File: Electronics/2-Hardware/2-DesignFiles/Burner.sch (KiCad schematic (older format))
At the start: 52 parts, among them P1 CONN_2, P2 CONN_2, P3 CONN_1, P4 CONN_01X03, P5 CONN_01X04, P6 CONN_1, P7 CONN_4, Q1 IRF9310, Q2 IRLML6402, Q3 IRL6342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

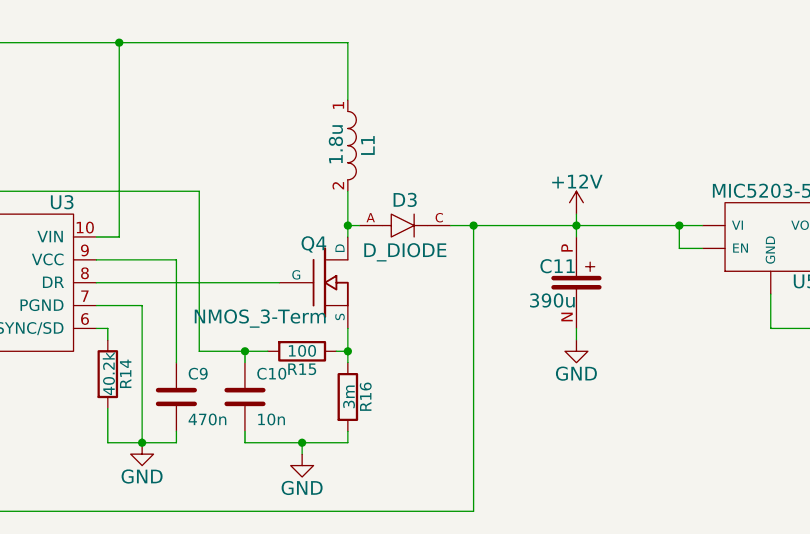
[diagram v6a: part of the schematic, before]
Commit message: Added diode and inductor for Boost converter
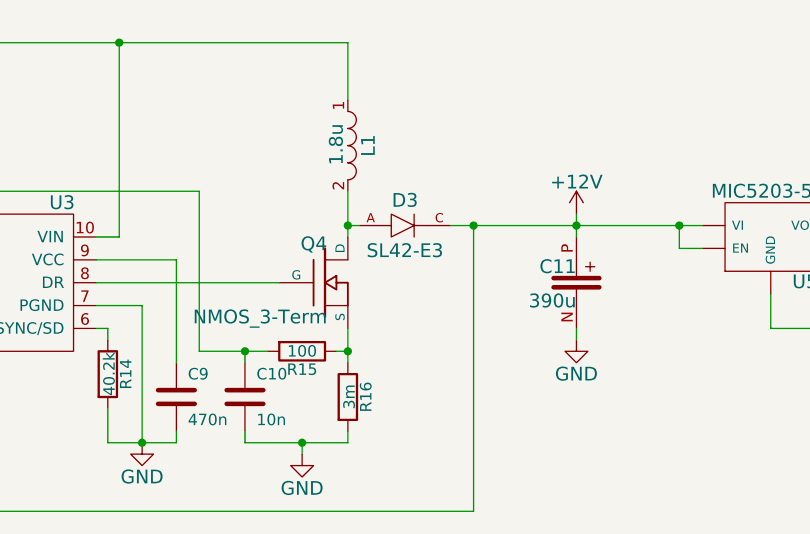
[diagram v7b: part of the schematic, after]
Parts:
- D3: value D_DIODE -> SL42-E3; footprint (none) -> Diodes:DIODE_DO214AB-SMC; DigikeyNumber (none) -> SL42-E3/57TGICT-ND; Manufacturer (none) -> Vishay; ManufacturerNumber (none) -> SL42-E3/57T
- L1: footprint (none) -> Inductors:IND_BOURNS_SRP1238A; DigikeyNumber (none) -> SRP1238A-1R8MCT-ND; Manufacturer (none) -> Bourns; ManufacturerNumber (none) -> SRP1238A-1R8M
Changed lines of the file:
@@
 P 7300 1600
 F 0 "D3" V 7190 1600 60  0000 C CNN
-F 1 "D_DIODE" V 7410 1600 60  0000 C CNN
-F 2 "" H 7300 1580 60  0001 C CNN
-F 3 "" H 7300 1580 60  0001 C CNN
+F 1 "SL42-E3" V 7410 1600 60  0000 C CNN
+F 2 "Diodes:DIODE_DO214AB-SMC" H 7300 1580 60  0001 C CNN
+F 3 "http://www.vishay.com/docs/88742/sl42.pdf" H 7300 1580 60  0001 C CNN
+F 4 "SL42-E3/57TGICT-ND" V 7300 1600 60  0001 C CNN "DigikeyNumber"
+F 5 "Vishay" V 7300 1600 60  0001 C CNN "Manufacturer"
+F 6 "SL42-E3/57T" V 7300 1600 60  0001 C CNN "ManufacturerNumber"
 	1    7300 1600
 	0    1    1    0
@@
 F 0 "L1" V 7140 1250 60  0000 C CNN
 F 1 "1.8u" V 7000 1255 60  0000 C CNN
-F 2 "" H 7050 1250 60  0001 C CNN
-F 3 "" H 7050 1250 60  0000 C CNN
+F 2 "Inductors:IND_BOURNS_SRP1238A" H 7050 1250 60  0001 C CNN
+F 3 "http://www.bourns.com/data/global/pdfs/SRP1238A.pdf" H 7050 1250 60  0001 C CNN
+F 4 "SRP1238A-1R8MCT-ND" V 7050 1250 60  0001 C CNN "DigikeyNumber"
+F 5 "Bourns" V 7050 1250 60  0001 C CNN "Manufacturer"
+F 6 "SRP1238A-1R8M" V 7050 1250 60  0001 C CNN "ManufacturerNumber"
 	1    7050 1250
 	1    0    0    -1

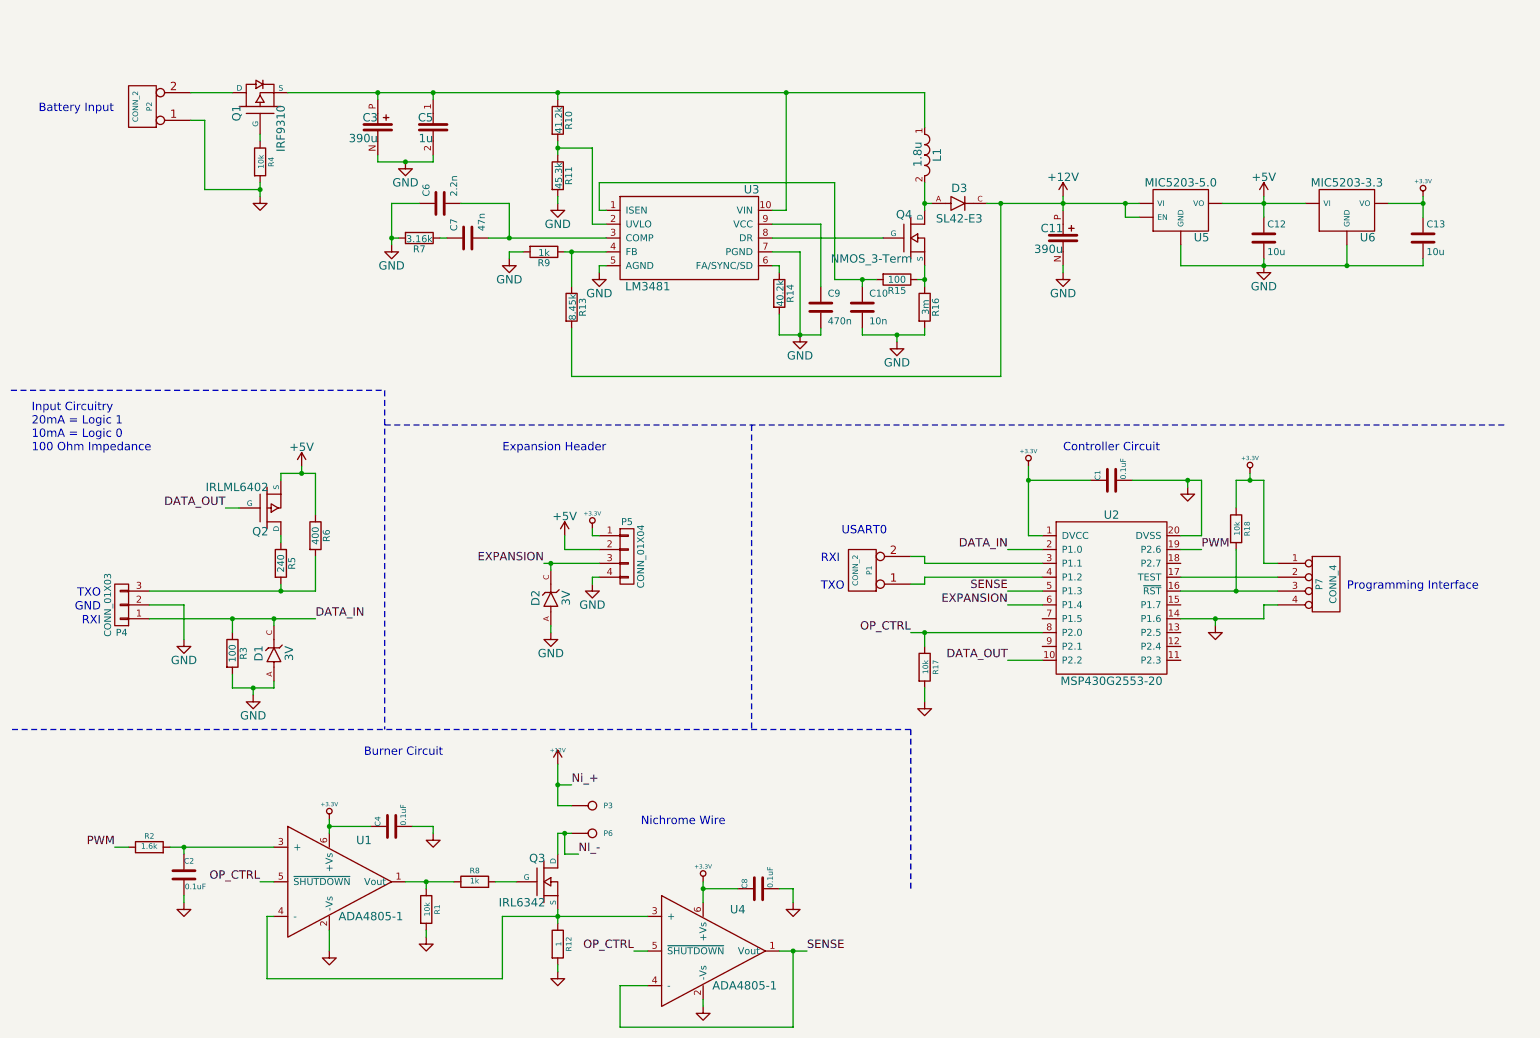
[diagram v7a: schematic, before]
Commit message: Updated schematic with LEDs, created board layout
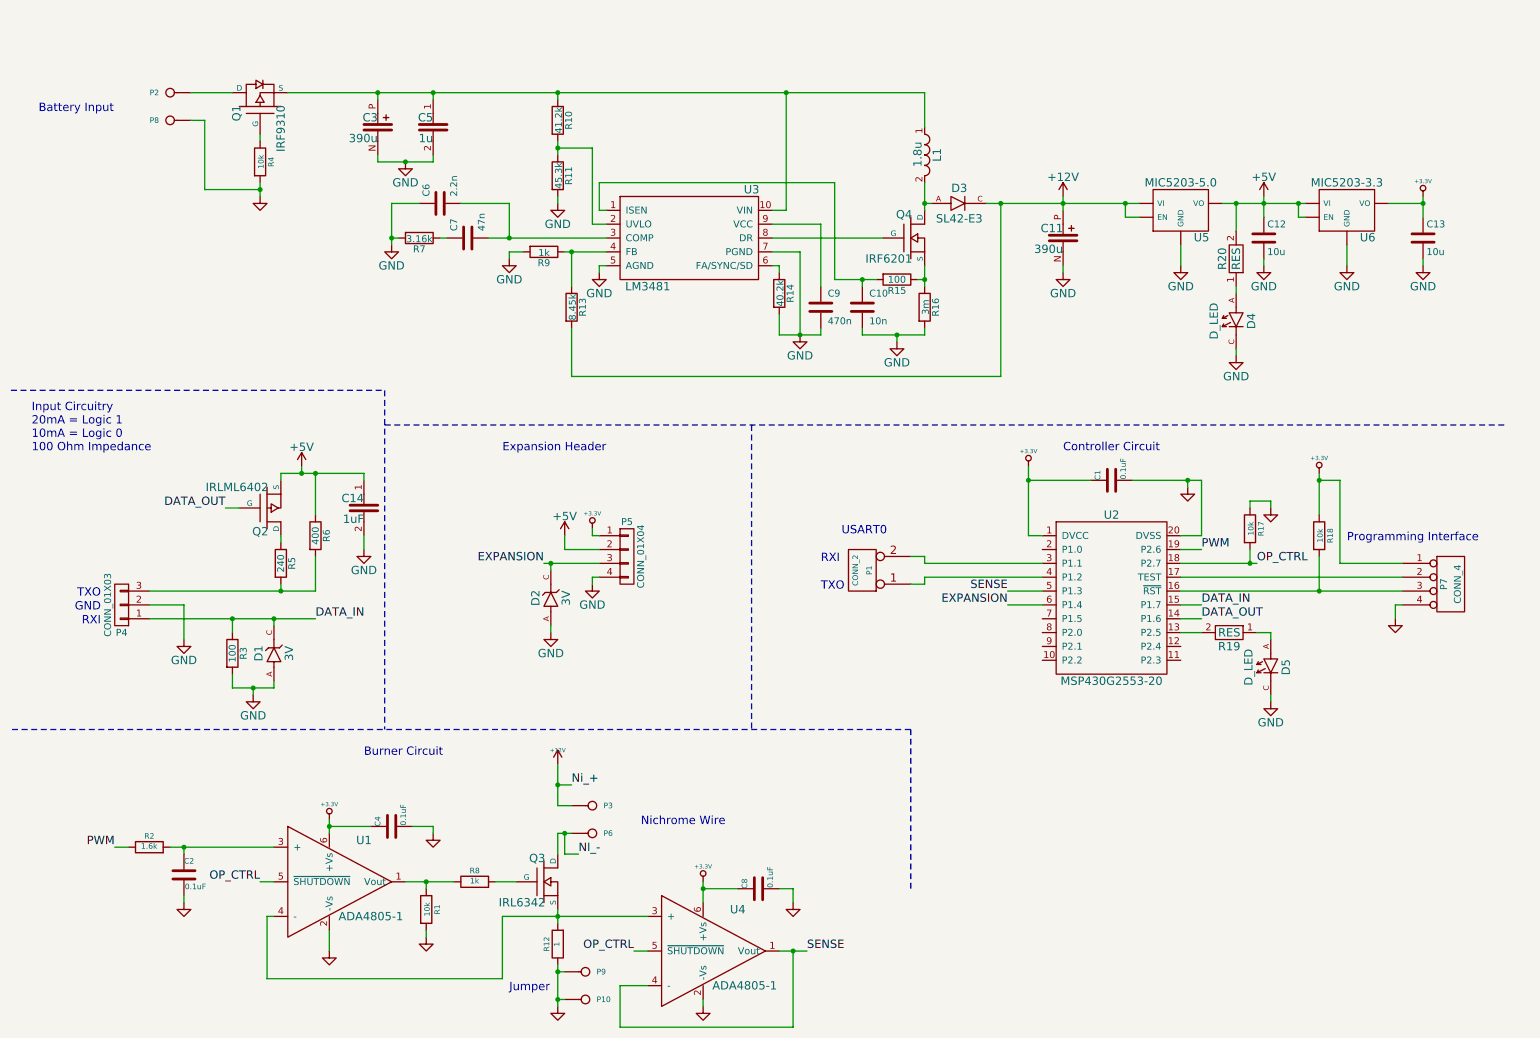
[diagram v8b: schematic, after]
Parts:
- removed P2: CONN_2, Footprints:CONN_1x2, symbol CONN_2
- removed U6: MIC5203-3.3, SMD:SOT-23-5, symbol LINEAR_REGULATOR
- added C14: 1uF, SMD:SMD_0805, symbol CAP
- added D4, D5: D_LED, LEDs:LED_1206, symbol D_LED
- added P10, P2, P8, P9: CONN_1, Connectors:CONN_2.54mm_1x1, symbol CONN_1
- added R19, R20: RES, SMD:SMD_0805, symbol RES
- added U6: MIC5203-3.3, SMD:SOT-23-5, symbol LINEAR_REGULATOR_EN
- C1, C10, C12, C13, C2, C4, C5, C6, C7, C8, C9: footprint Capacitors_SMD:C_0805_HandSoldering -> SMD:SMD_0805
- D1, D2: footprint SMD:DIODE_SOT-23-3 -> Diodes:DIODE_SOT-23-3
- P1: footprint Footprints:CONN_1x2 -> Connectors:CONN_2.54mm_1x2
- P3, P6: footprint Footprints:CONN_1x1 -> Connectors:CONN_2.54mm_1x1
- P4: footprint Footprints:CONN_1x2 -> Connectors:CONN_2.54mm_1x3
- P5: footprint Footprints:CONN_1x2 -> Connectors:CONN_2.00mm_1x4
- P7: footprint Footprints:CONN_1x4 -> Connectors:CONN_2.54mm_1x4
- Q4: value NMOS_3-Term -> IRF6201; footprint (none) -> Transistors:TRANS_SO_4.0mm_1.27mm_8; DigikeyNumber (none) -> IRF6201TRPBFCT-ND; Manufacturer (none) -> International Rectifier; ManufacturerNumber (none) -> IRF6201TRPBF
- R1, R10, R11, R13, R14, R15, R17, R18, R2, R3, R4, R5, R6, R7, R8, R9: footprint Resistors_SMD:R_0805_HandSoldering -> SMD:SMD_0805
- R12: footprint SMD:RES_D2PACK -> Resistors:RES_D2PACK
- R16: footprint Footprints:SM2010 -> SMD:SMD_2010
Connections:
- net +3.3V: now also U6.5 (VO)
- net +5V: now also C14.1, R20.2, U6.1 (VI), U6.3 (EN)
- net DATA_IN: now also U2.15 (P1.7); no longer U2.2 (P1.0)
- net DATA_OUT: now also U2.14 (P1.6); no longer U2.10 (P2.2)
- net GND: now also R12.1, R17.1, C14.2, D4.C, D5.C, P10.1, P8.1, P9.1, U6.2 (GND); no longer R12.2, R17.2, U2.14 (P1.6)
- net OP_CTRL: now also R17.2, U2.18 (P2.7); no longer R17.1, U2.8 (P2.0)
- net at U2.13 (P2.5): now also R19.2
- net at Q1.D: now also P2.1
- net at Q3.S, U1.4 (-), U4.3 (+): now also R12.2; no longer R12.1
- new net: D4.A, R20.1
- new net: D5.A, R19.1
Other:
- note added: "Jumper"
- moved on the sheet: P7, R17, R18
